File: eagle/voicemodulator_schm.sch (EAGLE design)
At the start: 36 parts, among them T1 2N5089, T2 2N5089, T3 2N5089, T4 2N5089

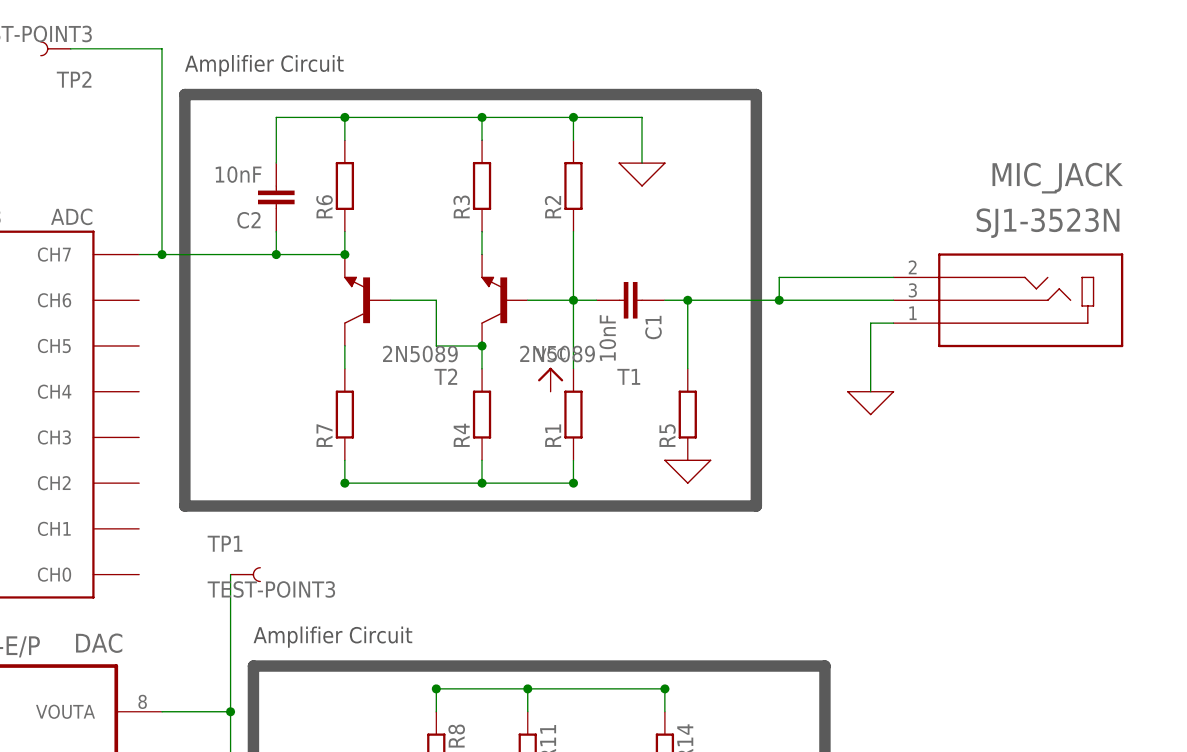
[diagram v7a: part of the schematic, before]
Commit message: Segmented input with 0 ohm resistors for w/ amp vs. not
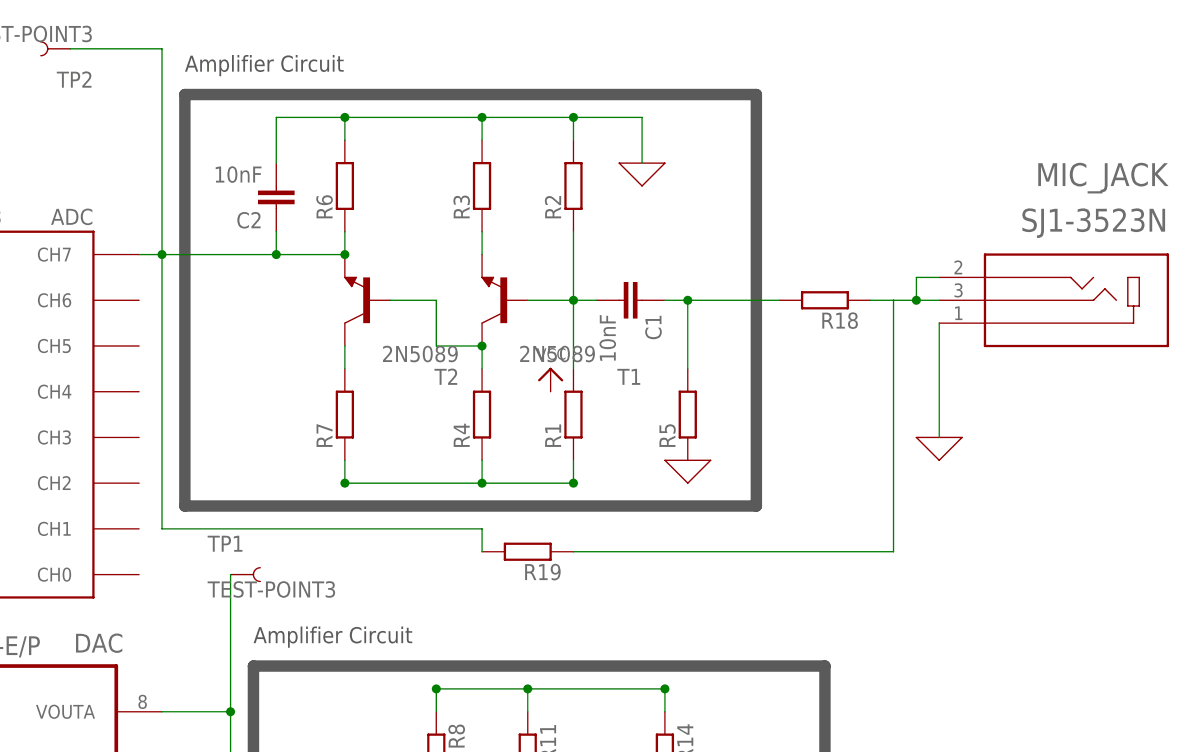
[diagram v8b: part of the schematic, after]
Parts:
- added R18, R19: (no value), resistor-shunt:SMR-WAV
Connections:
- new net N$24: MIC_JACK.2, MIC_JACK.3, R18.2, R19.2
- net N$1: now also R18.1; no longer MIC_JACK.2, MIC_JACK.3
- net N$5: now also R19.1
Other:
- moved on the sheet: MIC_JACK
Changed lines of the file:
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@@
 <part name="R17" library="resistor-shunt" library_urn="urn:adsk.eagle:library:346" deviceset="SMR-WAV" device="" package3d_urn="urn:adsk.eagle:package:25223/1"/>
 <part name="IC1" library="voicemod_parts" deviceset="ATMEGA48/88/168/328-PU(DIP28)" device="PU"/>
+<part name="R18" library="resistor-shunt" library_urn="urn:adsk.eagle:library:346" deviceset="SMR-WAV" device="" package3d_urn="urn:adsk.eagle:package:25223/1"/>
+<part name="R19" library="resistor-shunt" library_urn="urn:adsk.eagle:library:346" deviceset="SMR-WAV" device="" package3d_urn="urn:adsk.eagle:package:25223/1"/>
 </parts>
 <sheets>
@@
 <attribute name="VALUE" x="68.58" y="83.82" size="1.778" layer="96" rot="R180"/>
 </instance>
-<instance part="MIC_JACK" gate="G$1" x="182.88" y="73.66" rot="R180">
-<attribute name="NAME" x="193.0489" y="88.89335" size="2.54221875" layer="95" rot="R180"/>
-<attribute name="VALUE" x="193.0453" y="83.8253" size="2.541340625" layer="96" rot="R180"/>
-</instance>
-<instance part="X_1" gate="G$1" x="165.1" y="63.5"/>
+<instance part="MIC_JACK" gate="G$1" x="187.96" y="73.66" rot="R180">
+<attribute name="NAME" x="198.1289" y="88.89335" size="2.54221875" layer="95" rot="R180"/>
+<attribute name="VALUE" x="198.1253" y="83.8253" size="2.541340625" layer="96" rot="R180"/>
+</instance>
+<instance part="X_1" gate="G$1" x="172.72" y="58.42"/>
 <instance part="X_2" gate="G$1" x="48.26" y="2.54"/>
 <instance part="P+1" gate="VCC" x="48.26" y="40.64">
@@
 <attribute name="VALUE" x="-12.7" y="31.75" size="2.54" layer="96" ratio="12"/>
 </instance>
+<instance part="R18" gate="G$1" x="160.02" y="73.66" rot="R180">
+<attribute name="NAME" x="163.83" y="72.2884" size="1.778" layer="95" rot="R180"/>
+<attribute name="VALUE" x="163.83" y="76.581" size="1.778" layer="96" rot="R180"/>
+</instance>
+<instance part="R19" gate="G$1" x="127" y="45.72" rot="R180">
+<attribute name="NAME" x="130.81" y="44.3484" size="1.778" layer="95" rot="R180"/>
+<attribute name="VALUE" x="130.81" y="48.641" size="1.778" layer="96" rot="R180"/>
+</instance>
 </instances>
 <busses>
@@
 <pinref part="MIC_JACK" gate="G$1" pin="1"/>
 <pinref part="X_1" gate="G$1" pin="0"/>
-<wire x1="167.64" y1="71.12" x2="165.1" y2="71.12" width="0.1524" layer="91"/>
-<wire x1="165.1" y1="71.12" x2="165.1" y2="63.5" width="0.1524" layer="91"/>
+<wire x1="172.72" y1="71.12" x2="172.72" y2="58.42" width="0.1524" layer="91"/>
 </segment>
 <segment>
@@
 <net name="N$1" class="0">
 <segment>
-<pinref part="MIC_JACK" gate="G$1" pin="2"/>
-<wire x1="167.64" y1="76.2" x2="154.94" y2="76.2" width="0.1524" layer="91"/>
-<wire x1="154.94" y1="76.2" x2="154.94" y2="73.66" width="0.1524" layer="91"/>
-<pinref part="MIC_JACK" gate="G$1" pin="3"/>
-<wire x1="154.94" y1="73.66" x2="167.64" y2="73.66" width="0.1524" layer="91"/>
-<wire x1="154.94" y1="73.66" x2="144.78" y2="73.66" width="0.1524" layer="91"/>
 <pinref part="C1" gate="G$1" pin="1"/>
 <pinref part="R5" gate="G$1" pin="1"/>
@@
 <wire x1="144.78" y1="73.66" x2="144.78" y2="66.04" width="0.1524" layer="91"/>
 <junction x="144.78" y="73.66"/>
-<junction x="154.94" y="73.66"/>
+<wire x1="154.94" y1="73.66" x2="144.78" y2="73.66" width="0.1524" layer="91"/>
+<pinref part="R18" gate="G$1" pin="1"/>
 </segment>
 </net>
@@
 <wire x1="86.36" y1="101.6" x2="76.2" y2="101.6" width="0.1524" layer="91"/>
 <junction x="86.36" y="78.74"/>
+<pinref part="R19" gate="G$1" pin="1"/>
+<wire x1="121.92" y1="45.72" x2="121.92" y2="48.26" width="0.1524" layer="91"/>
+<wire x1="121.92" y1="48.26" x2="86.36" y2="48.26" width="0.1524" layer="91"/>
+<wire x1="86.36" y1="48.26" x2="86.36" y2="78.74" width="0.1524" layer="91"/>
 </segment>
 </net>
@@
 </segment>
 </net>
+<net name="N$24" class="0">
+<segment>
+<pinref part="MIC_JACK" gate="G$1" pin="3"/>
+<pinref part="MIC_JACK" gate="G$1" pin="2"/>
+<wire x1="172.72" y1="76.2" x2="170.18" y2="76.2" width="0.1524" layer="91"/>
+<wire x1="170.18" y1="76.2" x2="170.18" y2="73.66" width="0.1524" layer="91"/>
+<wire x1="170.18" y1="73.66" x2="172.72" y2="73.66" width="0.1524" layer="91"/>
+<junction x="170.18" y="73.66"/>
+<wire x1="170.18" y1="73.66" x2="167.64" y2="73.66" width="0.1524" layer="91"/>
+<pinref part="R18" gate="G$1" pin="2"/>
+<wire x1="167.64" y1="73.66" x2="165.1" y2="73.66" width="0.1524" layer="91"/>
+<wire x1="167.64" y1="73.66" x2="167.64" y2="45.72" width="0.1524" layer="91"/>
+<pinref part="R19" gate="G$1" pin="2"/>
+<wire x1="132.08" y1="45.72" x2="167.64" y2="45.72" width="0.1524" layer="91"/>
+</segment>
+</net>
